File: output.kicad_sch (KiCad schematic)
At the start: 30 parts, among them J10 Wire_Solder_2Pin, Q7 NVMFS5C468NL-HXY, Q8 NVMFS5C468NL-HXY, U10 INA281A3, U4 LM5109BMA

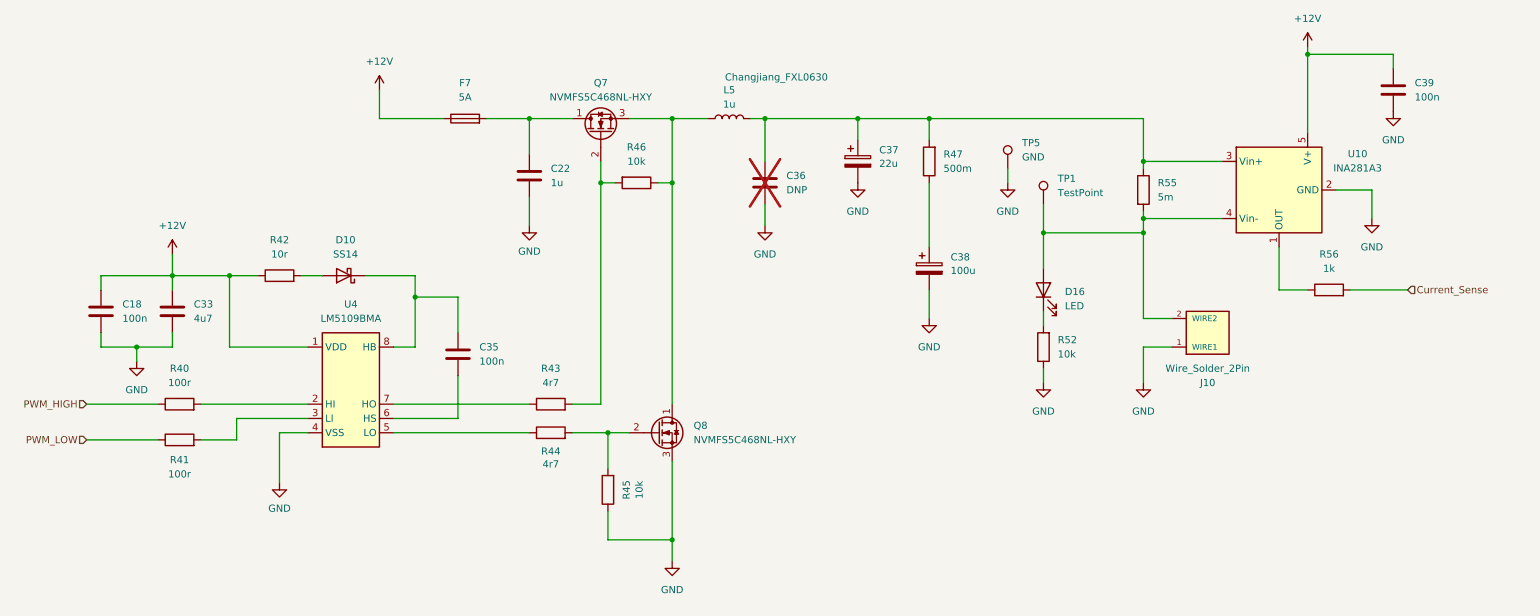
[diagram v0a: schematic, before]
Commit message: changed I2C temp sensor to thermistor
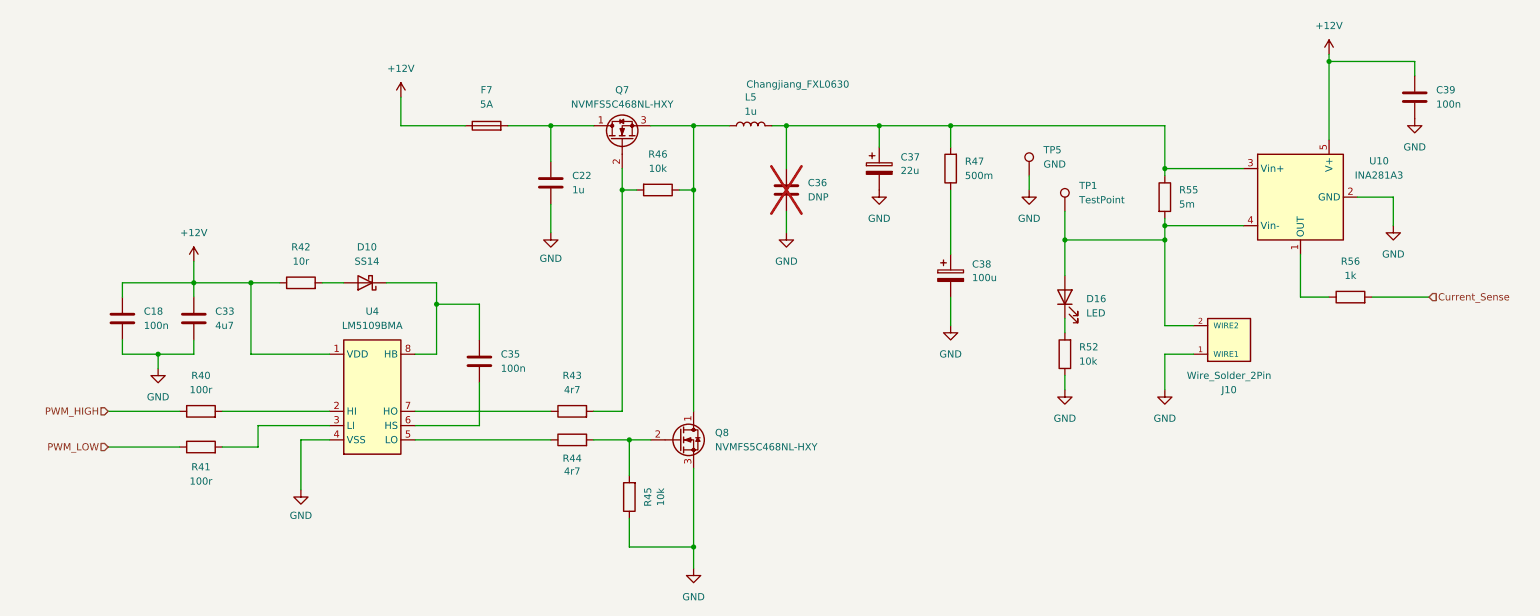
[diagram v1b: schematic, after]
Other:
- moved on the sheet: C18, C22, C33, C35, C36, C37, C38, C39, D10, D16, F7, J10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

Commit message: Placed designators
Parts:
- renumbered C22 to C30, C39 to C31, C18 to C34, C35 to C37, C38 to C41, C37 to C42, C36 to C43, D16 to D10, D10 to D11, F7 to F5, J10 to J12, L5 to L4, Q7 to Q8, Q8 to Q9, R52 to R34, R43 to R35, R46 to R38, R42 to R39, R55 to R42, R40 to R43, R47 to R45, R41 to R47, R44 to R50, R45 to R51, R56 to R76, TP5 to TP7, TP1 to TP8, U4 to U10, U10 to U8

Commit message: generated production files
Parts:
- R34, R38, R51: now not fitted
- R42: LCSC Part # C7419996 -> C253508
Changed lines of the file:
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@@
 			)
 		)
-		(property "LCSC Part #" "C7419996"
+		(property "LCSC Part #" "C253508"
 			(at 217.17 49.53 0)
 			(hide yes)
@@
 		(on_board yes)
 		(in_pos_files yes)
-		(dnp no)
+		(dnp yes)
 		(property "Reference" "R51"
 			(at 125.222 102.87 90)
@@
 		(on_board yes)
 		(in_pos_files yes)
-		(dnp no)
+		(dnp yes)
 		(fields_autoplaced yes)
 		(property "Reference" "R38"
@@
 		(on_board yes)
 		(in_pos_files yes)
-		(dnp no)
+		(dnp yes)
 		(fields_autoplaced yes)
 		(property "Reference" "R34"

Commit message: Fixed DNP parts on BOM
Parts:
- R34, R38, R51: now fitted
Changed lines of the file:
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@@
 		(on_board yes)
 		(in_pos_files yes)
-		(dnp yes)
+		(dnp no)
 		(property "Reference" "R51"
 			(at 125.222 102.87 90)
@@
 		(on_board yes)
 		(in_pos_files yes)
-		(dnp yes)
+		(dnp no)
 		(fields_autoplaced yes)
 		(property "Reference" "R38"
@@
 		(on_board yes)
 		(in_pos_files yes)
-		(dnp yes)
+		(dnp no)
 		(fields_autoplaced yes)
 		(property "Reference" "R34"
